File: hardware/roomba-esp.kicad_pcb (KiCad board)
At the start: 2 copper layers, 33 x 40 mm, 10 parts, among them P1 CONN_01X07, P2 CONN_02X10, P3 CONN_01X04, U1 ESP-12E, U2 LM2596_module

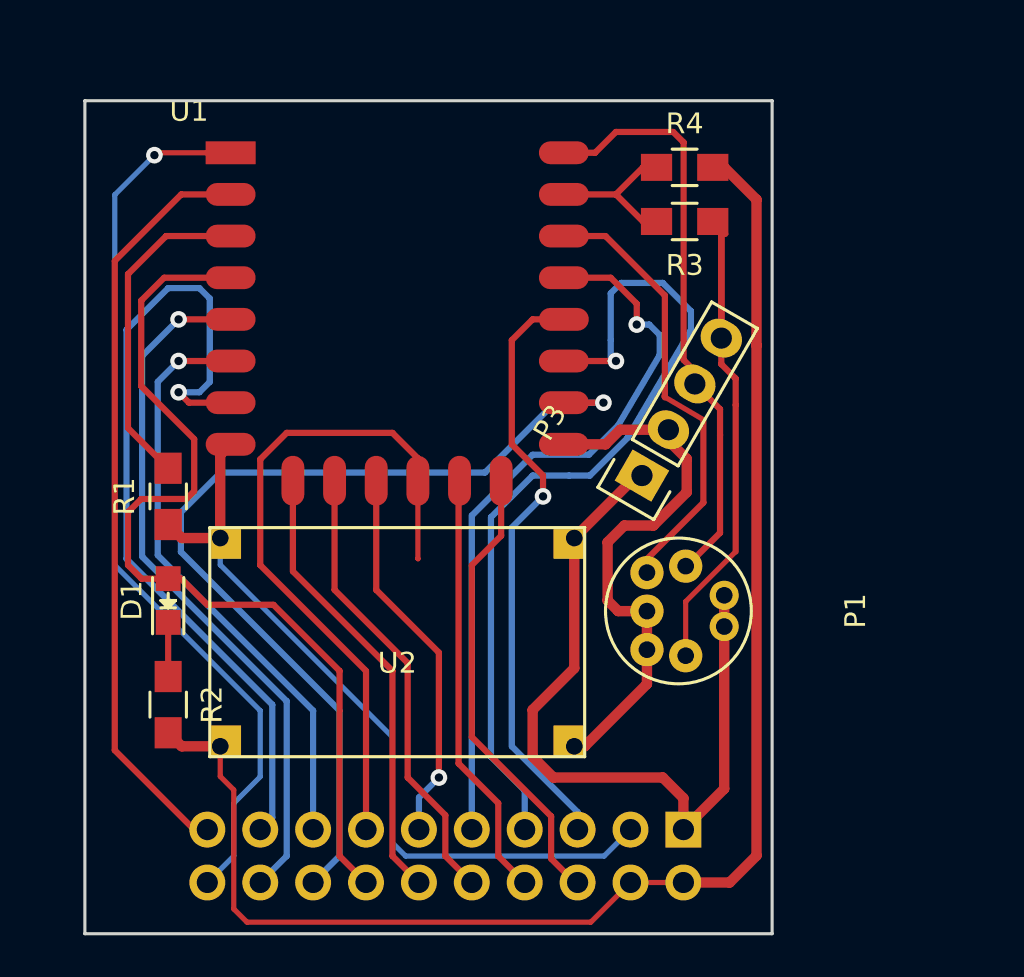
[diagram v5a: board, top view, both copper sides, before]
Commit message: added some keepout areas to increases manufacture reliability
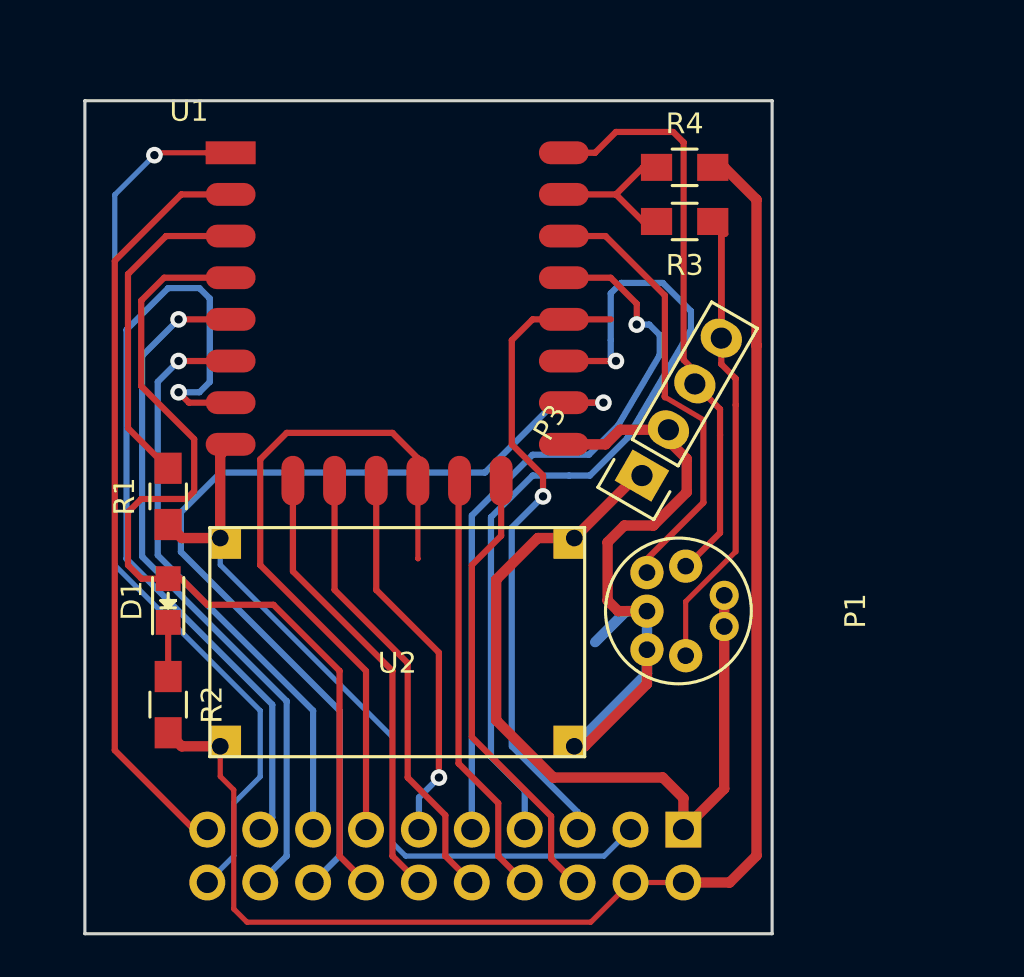
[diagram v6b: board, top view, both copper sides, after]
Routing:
- net GND: track 98.4 -> 107.6 mm
- net /VBat: track 37.8 -> 40.3 mm
- net /GPIO0: track 29.8 -> 32.1 mm
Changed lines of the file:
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@@
     (links 42)
     (no_connects 0)
-    (area 176.924999 91.924999 210.075001 132.075001)
+    (area 165.000001 85.773799 215.025 140.425001)
     (thickness 1.6)
     (drawings 6)
-    (tracks 250)
+    (tracks 255)
     (zones 0)
     (modules 10)
@@
     (31 B.Cu signal)
     (32 B.Adhes user)
-    (33 F.Adhes user hide)
+    (33 F.Adhes user)
     (34 B.Paste user)
     (35 F.Paste user)
@@
   (segment (start 189.23 128.27) (end 189.23 119.38) (width 0.3) (layer F.Cu) (net 1))
   (segment (start 181 119.65) (end 181 117.04902) (width 0.3) (layer F.Cu) (net 2) (status 30))
-  (segment (start 203.75 110) (end 203.5 110) (width 0.5) (layer F.Cu) (net 3) (status C00000))
-  (segment (start 203.5 110) (end 200.5 113) (width 0.5) (layer F.Cu) (net 3) (status C00000))
+  (segment (start 200.5 113) (end 198.75 113) (width 0.5) (layer F.Cu) (net 3))
+  (segment (start 205.74 125.49) (end 204.75 124.5) (width 0.5) (layer F.Cu) (net 3))
+  (segment (start 204.75 124.5) (end 199.5 124.5) (width 0.5) (layer F.Cu) (net 3))
+  (segment (start 205.74 125.49) (end 205.74 127) (width 0.5) (layer F.Cu) (net 3) (status 10))
+  (segment (start 196.75 121.75) (end 199.5 124.5) (width 0.5) (layer F.Cu) (net 3))
+  (segment (start 196.75 115) (end 196.75 121.75) (width 0.5) (layer F.Cu) (net 3))
+  (segment (start 198.75 113) (end 196.75 115) (width 0.5) (layer F.Cu) (net 3))
+  (segment (start 203.75 110) (end 203.5 110) (width 0.5) (layer F.Cu) (net 3))
+  (segment (start 203.5 110) (end 200.5 113) (width 0.5) (layer F.Cu) (net 3))
   (segment (start 200.5 113) (end 200.5 112.75) (width 0.5) (layer F.Cu) (net 3) (status 30))
-  (segment (start 205.74 127) (end 205.74 125.49) (width 0.5) (layer F.Cu) (net 3) (status 10))
-  (segment (start 200.5 119.25) (end 200.5 113) (width 0.5) (layer F.Cu) (net 3) (status 20))
-  (segment (start 198.5 121.25) (end 200.5 119.25) (width 0.5) (layer F.Cu) (net 3))
-  (segment (start 198.5 123.5) (end 198.5 121.25) (width 0.5) (layer F.Cu) (net 3))
-  (segment (start 199.5 124.5) (end 198.5 123.5) (width 0.5) (layer F.Cu) (net 3))
-  (segment (start 204.75 124.5) (end 199.5 124.5) (width 0.5) (layer F.Cu) (net 3))
-  (segment (start 205.74 125.49) (end 204.75 124.5) (width 0.5) (layer F.Cu) (net 3))
   (segment (start 207.7 117.25) (end 207.7 125.04) (width 0.5) (layer F.Cu) (net 3) (status 10))
   (segment (start 207.7 125.04) (end 205.74 127) (width 0.5) (layer F.Cu) (net 3) (status 20))
   (segment (start 207.7 115.75) (end 207.7 117.25) (width 0.5) (layer F.Cu) (net 3) (status 30))
   (segment (start 200.5 113) (end 200.63 113) (width 0.25) (layer F.Cu) (net 3) (status 30))
-  (segment (start 205.02 107.800295) (end 205.02 108.32) (width 0.5) (layer F.Cu) (net 4) (status C00000))
-  (segment (start 205.02 108.32) (end 205.9 109.2) (width 0.5) (layer F.Cu) (net 4) (status 400000))
-  (segment (start 202.61 116.51) (end 203.99 116.51) (width 0.5) (layer F.Cu) (net 4) (status 800000))
+  (segment (start 203.99 116.51) (end 202.99 116.51) (width 0.5) (layer B.Cu) (net 4) (status 400000))
+  (segment (start 202.99 116.51) (end 201.5 118) (width 0.5) (layer B.Cu) (net 4))
+  (segment (start 203.99 118.36) (end 203.99 119.51) (width 0.5) (layer B.Cu) (net 4))
+  (segment (start 203.99 119.51) (end 200.5 123) (width 0.5) (layer B.Cu) (net 4))
+  (segment (start 203.99 116.51) (end 203.99 118.36) (width 0.5) (layer B.Cu) (net 4))
+  (segment (start 205.02 107.800295) (end 205.02 108.32) (width 0.5) (layer F.Cu) (net 4))
+  (segment (start 205.02 108.32) (end 205.9 109.2) (width 0.5) (layer F.Cu) (net 4))
+  (segment (start 202.61 116.51) (end 203.99 116.51) (width 0.5) (layer F.Cu) (net 4))
   (segment (start 202.1 116) (end 202.61 116.51) (width 0.5) (layer F.Cu) (net 4))
   (segment (start 202.1 113.2) (end 202.1 116) (width 0.5) (layer F.Cu) (net 4))
@@
   (segment (start 205.9 110.8) (end 204.3 112.4) (width 0.5) (layer F.Cu) (net 4))
   (segment (start 205.9 109.2) (end 205.9 110.8) (width 0.5) (layer F.Cu) (net 4))
-  (segment (start 200 108.5) (end 202 108.5) (width 0.5) (layer F.Cu) (net 4) (status 400000))
-  (segment (start 202.699705 107.800295) (end 205.02 107.800295) (width 0.5) (layer F.Cu) (net 4) (status 800000))
+  (segment (start 200 108.5) (end 202 108.5) (width 0.5) (layer F.Cu) (net 4))
+  (segment (start 202.699705 107.800295) (end 205.02 107.800295) (width 0.5) (layer F.Cu) (net 4))
   (segment (start 202 108.5) (end 202.699705 107.800295) (width 0.5) (layer F.Cu) (net 4))
-  (segment (start 203.99 118.36) (end 203.99 116.51) (width 0.5) (layer F.Cu) (net 4))
   (segment (start 200.5 123) (end 201 123) (width 0.5) (layer F.Cu) (net 4))
   (segment (start 201 123) (end 203.99 120.01) (width 0.5) (layer F.Cu) (net 4))
@@
   (segment (start 183.5 113) (end 181.65 113) (width 0.5) (layer F.Cu) (net 5) (status 30))
   (segment (start 181.65 113) (end 181 112.35) (width 0.5) (layer F.Cu) (net 5) (status 30))
+  (segment (start 200 102.5) (end 202.25 102.5) (width 0.3) (layer F.Cu) (net 6))
   (segment (start 200.66 127) (end 200.66 126.16) (width 0.3) (layer B.Cu) (net 6) (status 30))
   (segment (start 200.66 126.16) (end 197.5 123) (width 0.3) (layer B.Cu) (net 6) (status 10))
@@
   (via (at 181.5 102.5) (size 0.8) (drill 0.4) (layers F.Cu B.Cu) (net 19))
   (segment (start 187.96 129.54) (end 189.23 128.27) (width 0.3) (layer B.Cu) (net 20))
-  (segment (start 201.9 106.5) (end 200 106.5) (width 0.3) (layer F.Cu) (net 20) (status 800000))
+  (segment (start 201.9 106.5) (end 200 106.5) (width 0.3) (layer F.Cu) (net 20))
   (via (at 201.9 106.5) (size 0.8) (drill 0.4) (layers F.Cu B.Cu) (net 20))
   (segment (start 199.57 106.5) (end 201.9 106.5) (width 0.3) (layer B.Cu) (net 20))
@@
   (segment (start 203.8 95.2) (end 204.45 95.2) (width 0.3) (layer F.Cu) (net 23) (status 30))
   (segment (start 200 96.5) (end 201.1 96.5) (width 0.3) (layer F.Cu) (net 23) (status 30))
-  (segment (start 207.56 103.400886) (end 207.56 98.21) (width 0.3) (layer F.Cu) (net 24) (status C00000))
-  (segment (start 207.56 98.21) (end 207.15 97.8) (width 0.3) (layer F.Cu) (net 24) (status C00000))
+  (segment (start 207.56 103.400886) (end 207.56 98.21) (width 0.3) (layer F.Cu) (net 24))
+  (segment (start 207.56 98.21) (end 207.15 97.8) (width 0.3) (layer F.Cu) (net 24))
   (segment (start 207.56 104.650886) (end 207.56 98.21) (width 0.3) (layer F.Cu) (net 24))
   (segment (start 207.56 98.21) (end 207.15 97.8) (width 0.3) (layer F.Cu) (net 24))
@@
   (segment (start 208.25 105.340886) (end 207.56 104.650886) (width 0.3) (layer F.Cu) (net 24))
   (segment (start 207.75 98.4) (end 207.15 97.8) (width 0.3) (layer F.Cu) (net 24) (status 30))
-  (segment (start 206.29 105.600591) (end 206.29 104.99) (width 0.3) (layer F.Cu) (net 25) (status C00000))
-  (segment (start 206.29 104.99) (end 205.75 104.45) (width 0.3) (layer F.Cu) (net 25) (status 400000))
+  (segment (start 206.29 105.600591) (end 206.29 104.99) (width 0.3) (layer F.Cu) (net 25))
+  (segment (start 206.29 104.99) (end 205.75 104.45) (width 0.3) (layer F.Cu) (net 25))
   (segment (start 205.75 94) (end 205.25 93.5) (width 0.3) (layer F.Cu) (net 25))
   (segment (start 205.25 93.5) (end 202.5 93.5) (width 0.3) (layer F.Cu) (net 25))
@@
   (segment (start 207.5 112.75) (end 207.5 108.060591) (width 0.3) (layer F.Cu) (net 25))
   (segment (start 205.9 114.35) (end 207.5 112.75) (width 0.3) (layer F.Cu) (net 25))
-  (segment (start 207.5 106.810591) (end 206.29 105.600591) (width 0.3) (layer F.Cu) (net 25) (status 800000))
+  (segment (start 207.5 106.810591) (end 206.29 105.600591) (width 0.3) (layer F.Cu) (net 25))
   (segment (start 205.85 114.35) (end 205.9 114.35) (width 0.3) (layer F.Cu) (net 25))
   (segment (start 200.8 94.5) (end 200 94.5) (width 0.3) (layer F.Cu) (net 25) (status 30))
@@
       )
     )
+  )
+  (zone (net 0) (net_name "") (layer F.Cu) (hatch edge 0.508)
+    (connect_pads (clearance 0.4))
+    (min_thickness 0.25)
+    (keepout (tracks allowed) (vias allowed) (copperpour not_allowed))
+    (fill (arc_segments 16) (thermal_gap 0.5) (thermal_bridge_width 0.5))
+    (polygon
+      (pts
+        (xy 186.25 107.5) (xy 197.75 107.5) (xy 197.75 93.25) (xy 202.75 93.25) (xy 202.75 113.5)
+        (xy 202.5 113.5) (xy 202.5 114) (xy 205.5 112.5) (xy 208.75 114) (xy 208.75 119.25)
+        (xy 205.75 120.75) (xy 203.25 119.25) (xy 202.5 116.5) (xy 202.5 115.5) (xy 198 115.5)
+        (xy 198 113.5) (xy 182.5 113.5) (xy 182.5 121.5) (xy 179.5 121.5) (xy 179.5 108)
+        (xy 182.182099 108) (xy 182 93.25) (xy 186.25 93.25) (xy 186.25 107.5)
+      )
+    )
+  )
+  (zone (net 0) (net_name "") (layer F.Cu) (hatch edge 0.508)
+    (connect_pads (clearance 0.4))
+    (min_thickness 0.25)
+    (keepout (tracks allowed) (vias allowed) (copperpour not_allowed))
+    (fill (arc_segments 16) (thermal_gap 0.5) (thermal_bridge_width 0.5))
+    (polygon
+      (pts
+        (xy 181 125.5) (xy 181 131) (xy 202.5 131) (xy 202.5 128.5) (xy 207.5 128.5)
+        (xy 207.5 125.5)
+      )
+    )
+  )
+  (zone (net 0) (net_name "") (layer B.Cu) (hatch edge 0.508)
+    (connect_pads (clearance 0.4))
+    (min_thickness 0.25)
+    (keepout (tracks allowed) (vias allowed) (copperpour not_allowed))
+    (fill (arc_segments 16) (thermal_gap 0.5) (thermal_bridge_width 0.5))
+    (polygon
+      (pts
+        (xy 202.5 114) (xy 202.5 116.5) (xy 203.25 119.25) (xy 205.75 120.75) (xy 208.75 119.25)
+        (xy 208.75 114) (xy 205.5 112.5)
+      )
+    )
+  )
+  (zone (net 0) (net_name "") (layer B.Cu) (hatch edge 0.508)
+    (connect_pads (clearance 0.4))
+    (min_thickness 0.25)
+    (keepout (tracks allowed) (vias allowed) (copperpour not_allowed))
+    (fill (arc_segments 16) (thermal_gap 0.5) (thermal_bridge_width 0.5))
+    (polygon
+      (pts
+        (xy 207.25 125.5) (xy 207.25 128.5) (xy 202.25 128.5) (xy 202.25 130.75) (xy 181.25 130.75)
+        (xy 181.25 125.5)
+      )
+    )

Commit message: added some keepout areas to increases manufacture reliability
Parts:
- added G***: LOGO, LOGO, B.Cu at (192.0, 98.0)
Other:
- board text added: "SNFI"
